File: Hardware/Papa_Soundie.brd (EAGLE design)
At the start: 38.1 x 63.5 mm, 82 parts, among them J1 Audio Jack, J2 MICRO-SD_CARD_SOCKET, U1 ATMEGA328P_TQFP, U2 VS1000D, U3 3.3V, U4 4MB Flash, Y1 12MHz, Y2 8MHz

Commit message: updated version no V10
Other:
- board text added: "v10"
- board text removed: "v03"
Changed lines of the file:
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@@
 <?xml version="1.0" encoding="utf-8"?>
 <!DOCTYPE eagle SYSTEM "eagle.dtd">
-<eagle version="8.6.1">
+<eagle version="7.2.0">
 <drawing>
 <settings>
 <setting alwaysvectorfont="no"/>
-<setting keepoldvectorfont="yes"/>
 <setting verticaltext="up"/>
 </settings>
@@
 SOUNDIE</text>
 <text x="5.953125" y="72.7075" size="1.778" layer="47" font="vector" ratio="15">All Units Inches</text>
-<text x="7.325625" y="62.49675" size="0.8128" layer="16" font="vector" ratio="25" rot="SMR0">v03</text>
+<text x="7.325625" y="62.49675" size="0.8128" layer="16" font="vector" ratio="25" rot="SMR0">v10</text>
 <wire x1="38.1" y1="63.5" x2="0" y2="63.5" width="0.2032" layer="20"/>
 <wire x1="0" y1="63.5" x2="0" y2="0" width="0.2032" layer="20"/>
@@
 <param name="dpMaxLengthDifference" value="10mm"/>
 <param name="dpGapFactor" value="2.5"/>
+<param name="checkGrid" value="0"/>
 <param name="checkAngle" value="1"/>
 <param name="checkFont" value="1"/>
 <param name="checkRestrict" value="1"/>
-<param name="checkStop" value="0"/>
-<param name="checkValues" value="0"/>
 <param name="useDiameter" value="13"/>
 <param name="maxErrors" value="50"/>

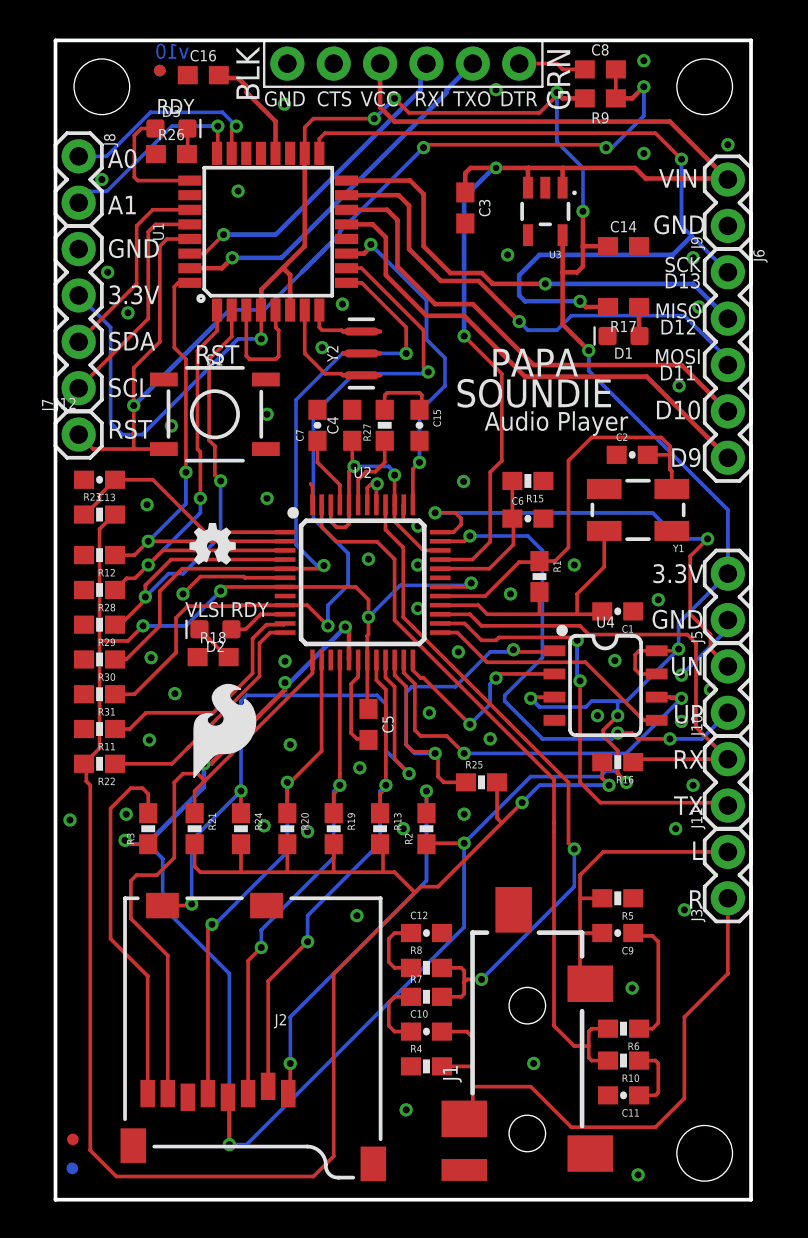
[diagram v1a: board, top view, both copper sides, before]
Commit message: updating silk, cleaning sch
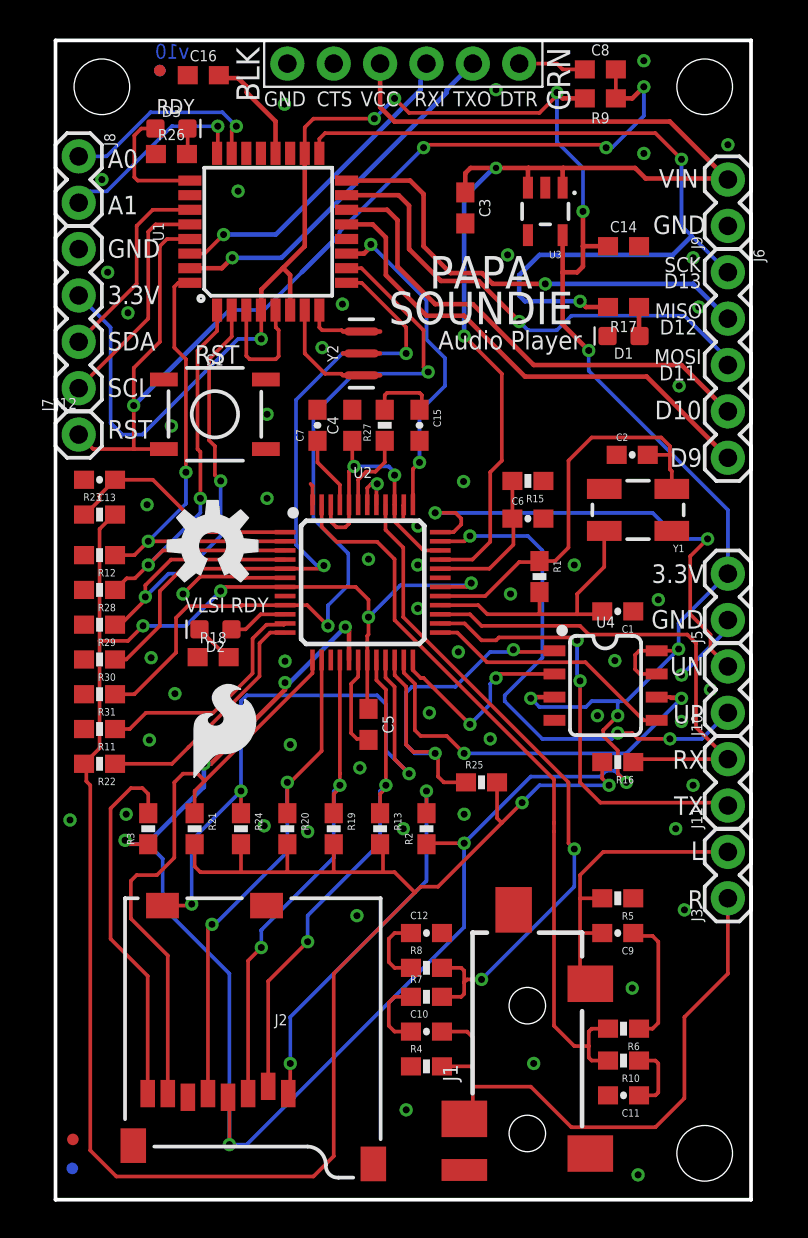
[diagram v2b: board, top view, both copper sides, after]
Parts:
- LOGO3: device SparkFun-Aesthetics:OSHW-LOGO-MINI -> SparkFun-Aesthetics:OSHW-LOGO-M
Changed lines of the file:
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@@
 <?xml version="1.0" encoding="utf-8"?>
 <!DOCTYPE eagle SYSTEM "eagle.dtd">
-<eagle version="7.2.0">
+<eagle version="7.7.0">
 <drawing>
 <settings>
@@
 <board>
 <plain>
-<text x="26.2255" y="46.609" size="1.524" layer="21" font="vector" ratio="20" distance="10" rot="R180" align="bottom-center">PAPA
+<text x="23.3045" y="51.689" size="1.778" layer="21" font="vector" ratio="20" distance="10" rot="R180" align="bottom-center">PAPA
 SOUNDIE</text>
 <text x="5.953125" y="72.7075" size="1.778" layer="47" font="vector" ratio="15">All Units Inches</text>
@@
 <dimension x1="0" y1="63.5" x2="38.1" y2="63.5" x3="19.05" y3="69.85" textsize="1.778" layer="47" unit="inch"/>
 <text x="2.8575" y="56.515" size="1.016" layer="21" font="vector" ratio="20">A0</text>
-<text x="31.3655" y="43.1445" size="1.016" layer="21" font="vector" ratio="15" rot="R180">Audio Player</text>
+<text x="28.8255" y="47.5895" size="1.016" layer="21" font="vector" ratio="15" rot="R180">Audio Player</text>
 <text x="15.5575" y="-24.13" size="1.778" layer="51" font="vector" ratio="15">Mary West</text>
 <dimension x1="35.56" y1="60.96" x2="38.1" y2="60.96" x3="36.83" y3="66.3575" textsize="1.778" layer="47" unit="inch"/>
@@
 <wire x1="2.54" y1="58.26125" x2="2.69875" y2="58.26125" width="0.2032" layer="49"/>
 <dimension x1="35.56" y1="2.54" x2="38.1" y2="2.54" x3="36.83" y3="-3.81" textsize="1.778" layer="47" unit="inch"/>
-<text x="11.6805" y="32.7305" size="0.8128" layer="21" font="vector" ratio="15" rot="R180">VLSI RDY</text>
+<text x="11.6805" y="32.9845" size="0.8128" layer="21" font="vector" ratio="20" rot="R180">VLSI RDY</text>
 <text x="2.8575" y="41.68775" size="1.016" layer="21" font="vector" ratio="20">RST</text>
 <text x="7.6165" y="60.2895" size="0.8128" layer="21" font="vector" ratio="15" rot="R180">RDY</text>
@@
 </element>
 <element name="J11" library="SparkFun-Connectors" package="1X02" value="" x="36.83" y="21.59" rot="R90"/>
-<element name="LOGO3" library="SparkFun-Aesthetics" package="OSHW-LOGO-MINI" value="OSHW-LOGOL" x="8.60425" y="35.814"/>
+<element name="LOGO3" library="SparkFun-Aesthetics" package="OSHW-LOGO-M" value="OSHW-LOGOL" x="8.60425" y="35.814"/>
 <element name="J5" library="SparkFun-Connectors" package="1X02" value="" x="36.83" y="31.75" rot="R90"/>
 <element name="J10" library="SparkFun-Connectors" package="1X02" value="" x="36.83" y="26.67" rot="R90"/>
@@
 <contactref element="U4" pad="8"/>
 <contactref element="U4" pad="7"/>
-<contactref element="U4" pad="3"/>
 <contactref element="J5" pad="2"/>
 <wire x1="5.08" y1="19.47" x2="4.025" y2="19.47" width="0.2032" layer="1"/>
@@
 <wire x1="4.7625" y1="41.91" x2="10.00125" y2="47.14875" width="0.2032" layer="16"/>
 <wire x1="18.57375" y1="60.325" x2="17.4625" y2="59.21375" width="0.2032" layer="16"/>
-<wire x1="27.33075" y1="27.52725" x2="26.0985" y2="27.52725" width="0.2032" layer="1"/>
 <wire x1="26.0985" y1="27.52725" x2="26.035" y2="27.46375" width="0.2032" layer="1"/>
 <wire x1="26.51125" y1="26.9875" x2="26.035" y2="27.46375" width="0.2032" layer="16"/>
@@
 <wire x1="16.0775" y1="29.56375" x2="16.0775" y2="31.1665" width="0.254" layer="1"/>
 <wire x1="16.0775" y1="31.1665" x2="15.875" y2="31.369" width="0.254" layer="1"/>
+<contactref element="U4" pad="3"/>
+<wire x1="27.33075" y1="27.52725" x2="26.035" y2="27.52725" width="0.254" layer="1"/>
+<wire x1="26.035" y1="27.52725" x2="26.035" y2="27.46375" width="0.254" layer="1"/>
 </signal>
 <signal name="AVDD">

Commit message: fixed DRC issues
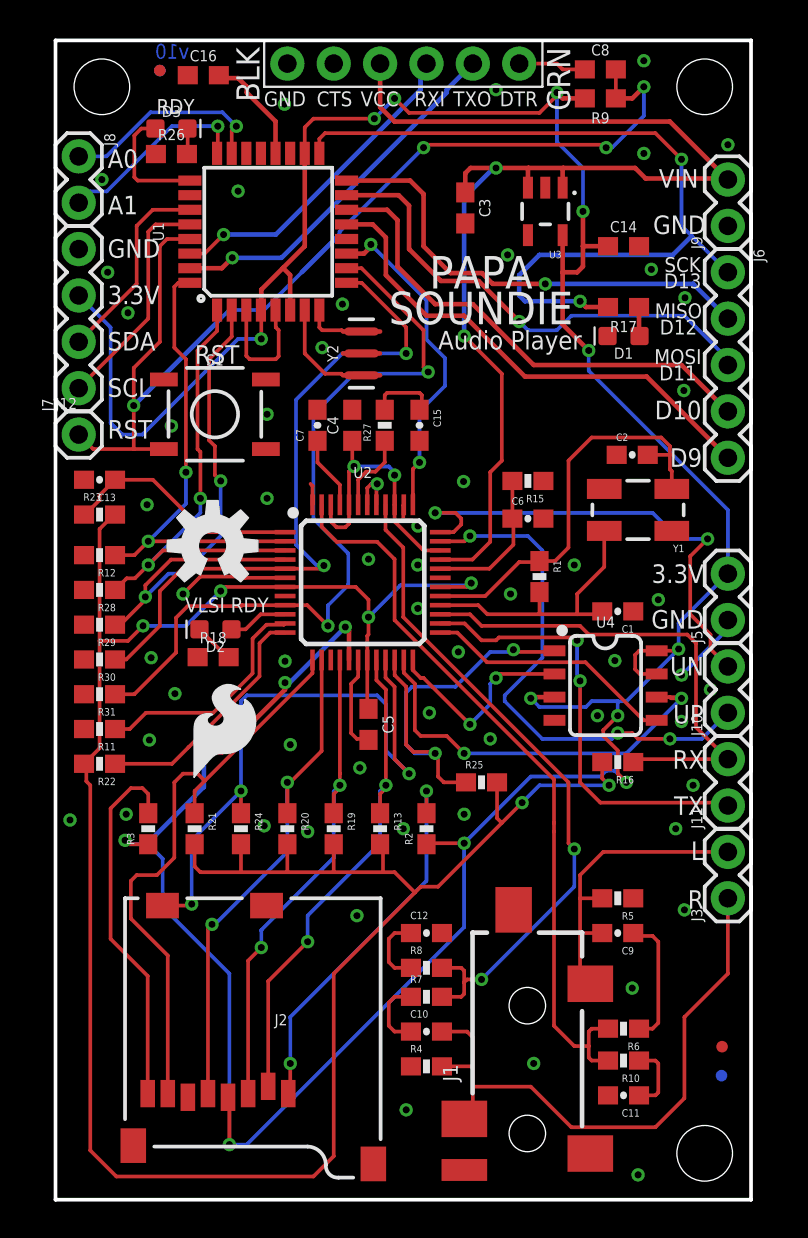
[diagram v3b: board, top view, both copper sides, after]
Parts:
- moved FD2 35.9 mm to (36.5, 8.38)
- moved FD4 35.9 mm to (36.5, 6.79)

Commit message: Fixing issues per QC Review
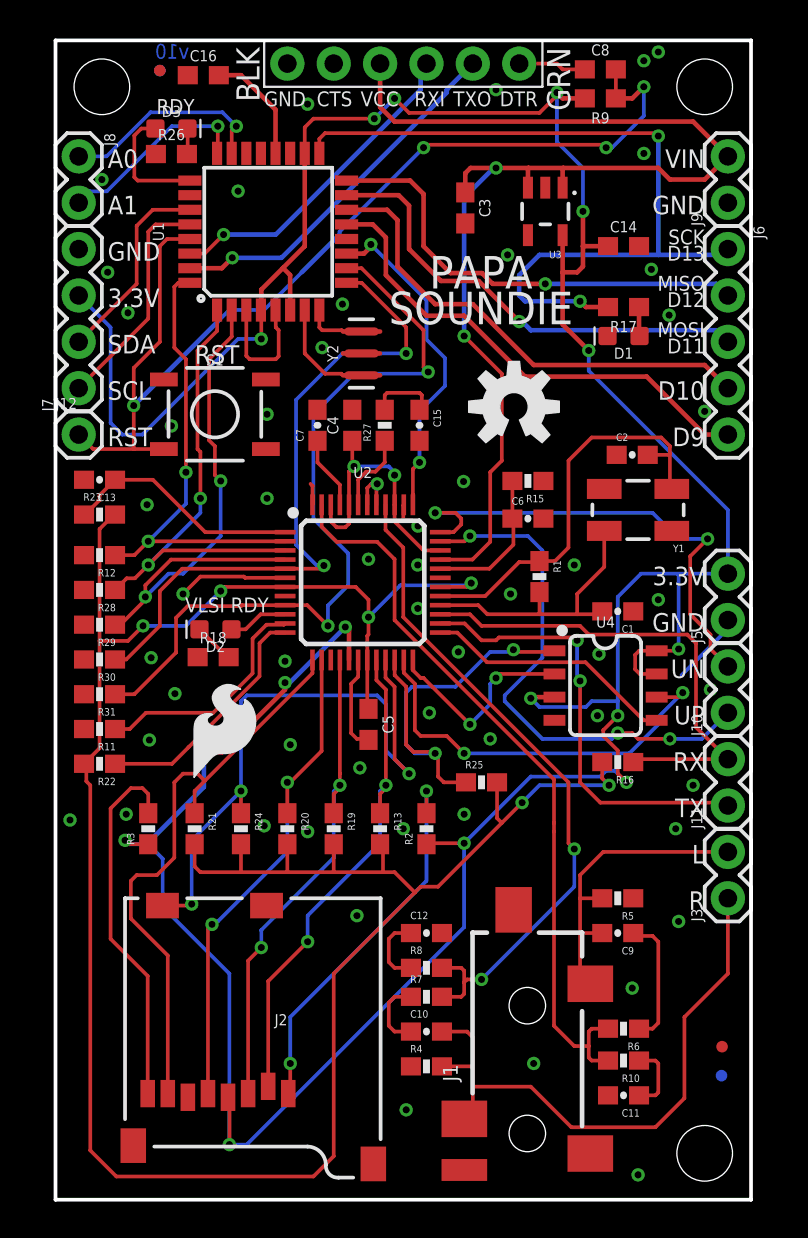
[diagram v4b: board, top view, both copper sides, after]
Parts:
- moved LOGO3 18.2 mm to (25.1, 43.4)
- moved LOGO6 1.59 mm to (30.9, 44.2)
- moved J6 1.27 mm to (36.8, 52.1)
- moved J9 1.27 mm to (36.8, 54.6)
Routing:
- net VCC: track 191.1 -> 197.8 mm
- net MOSI: track 27.0 -> 25.6 mm
- net SCK: track 45.2 -> 44.3 mm
- net MISO: track 25.7 -> 25.2 mm
- net D10: track 26.9 -> 26.4 mm
- net D9: track 27.4 -> 26.9 mm
- net GND: vias 57 -> 55
